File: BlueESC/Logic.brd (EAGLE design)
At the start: 24.4 x 27.5 mm, 33 parts, among them U1 ATMEGA168, U2 V_REG_LDOSMD, Y1 RESONATORSMD

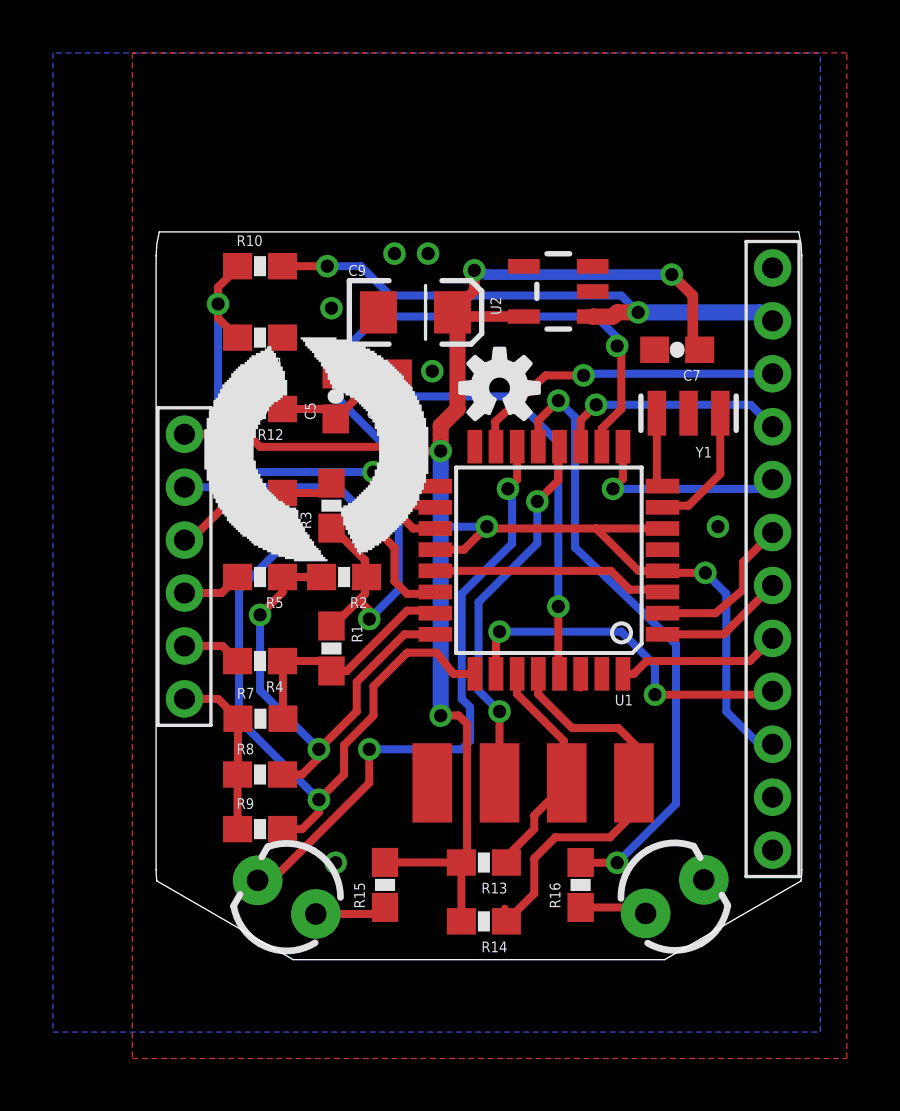
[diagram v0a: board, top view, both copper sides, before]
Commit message: Switch to SMT LEDs.
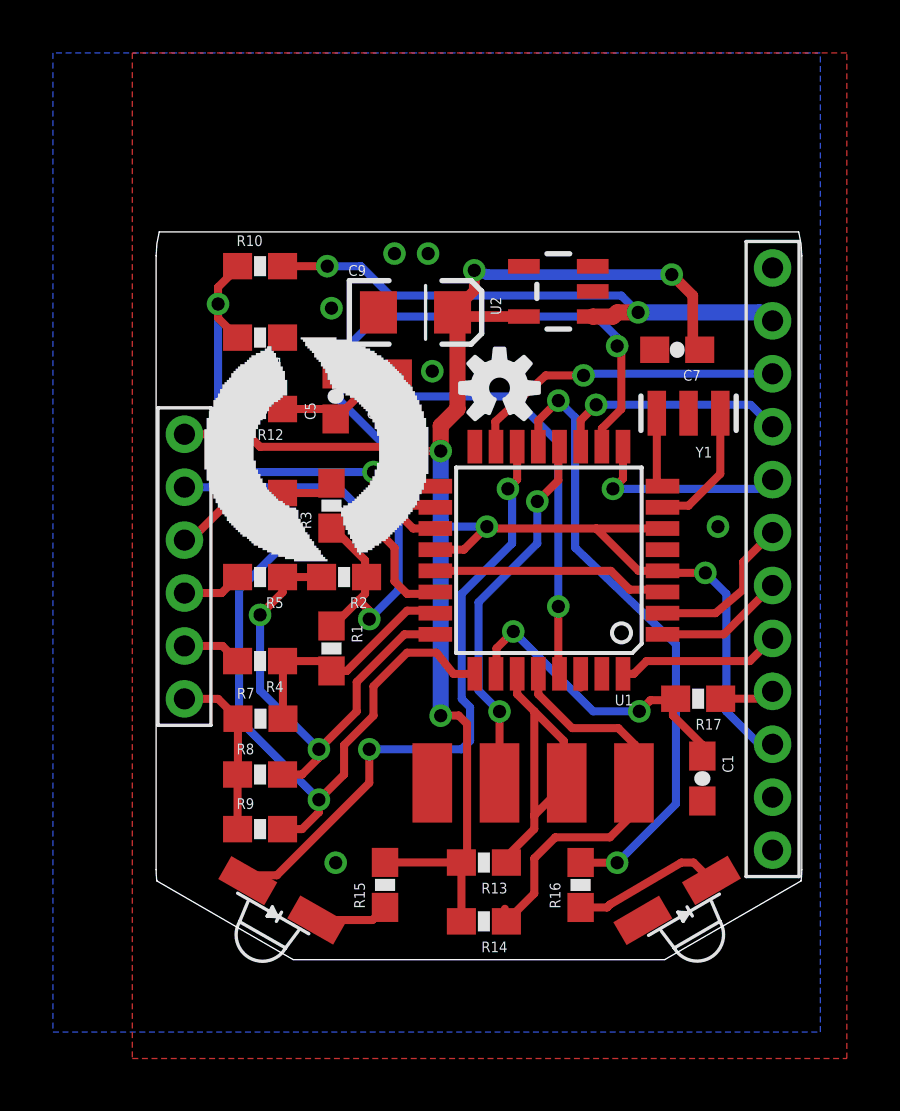
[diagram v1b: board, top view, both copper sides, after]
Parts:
- added C1: 1uF, SparkFun-Capacitors:0603-CAP
- added R17: 47K, SparkFun:0603-RES
- LED1: value RED -> BLUE; device SparkFun:LED3MM -> BR-Eagle-Library:SMT-LED-3X2-RA
- LED2: value BLUE -> RED; device SparkFun:LED3MM -> BR-Eagle-Library:SMT-LED-3X2-RA
- R15: value 2.2K -> 1K
- R16: value 150 -> 10K
- moved LED1 14.8 mm to (4.76, 5.24), turned to 150.3 degrees
- moved LED2 14.8 mm to (19.7, 5.24), turned to 210.2 degrees
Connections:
- new net CURRENT_ADC_FILTERED: C1.1, R17.2, U1.26
- net CURRENT_ADC: now also R17.1; no longer U1.26
- net GND: now also C1.2, LED2.2; no longer LED1.K
- net LED_STATUS: now also LED1.2; no longer LED2.K
- net N$16: now also LED1.1; no longer LED2.A
- net N$3: now also LED2.1; no longer LED1.A
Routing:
- net CURRENT_ADC_FILTERED: track 0.00 -> 12.0 mm, vias 0 -> 2
- net CURRENT_ADC: track 13.7 -> 2.08 mm, vias 2 -> 0
- net SDA: track 9.98 -> 13.9 mm
- net N$3: track 2.55 -> 5.70 mm
- net LED_STATUS: track 23.3 -> 24.2 mm
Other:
- board text added: "8/15"
- board text added: "BLUEESC-ELEC-LOGIC-R1.1"
- board text added: "Designed by R. Jehangir"
- board text added: "ERROR"
- board text added: "STATUS"
- board text added: "rev6"
- board text removed: "1/15"
- board text removed: "BLUESC-ELEC-LOGIC-X1B"
- board text removed: "Designed by R.J."
- board text removed: "rev5"

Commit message: Added PWM pull-down resistor.
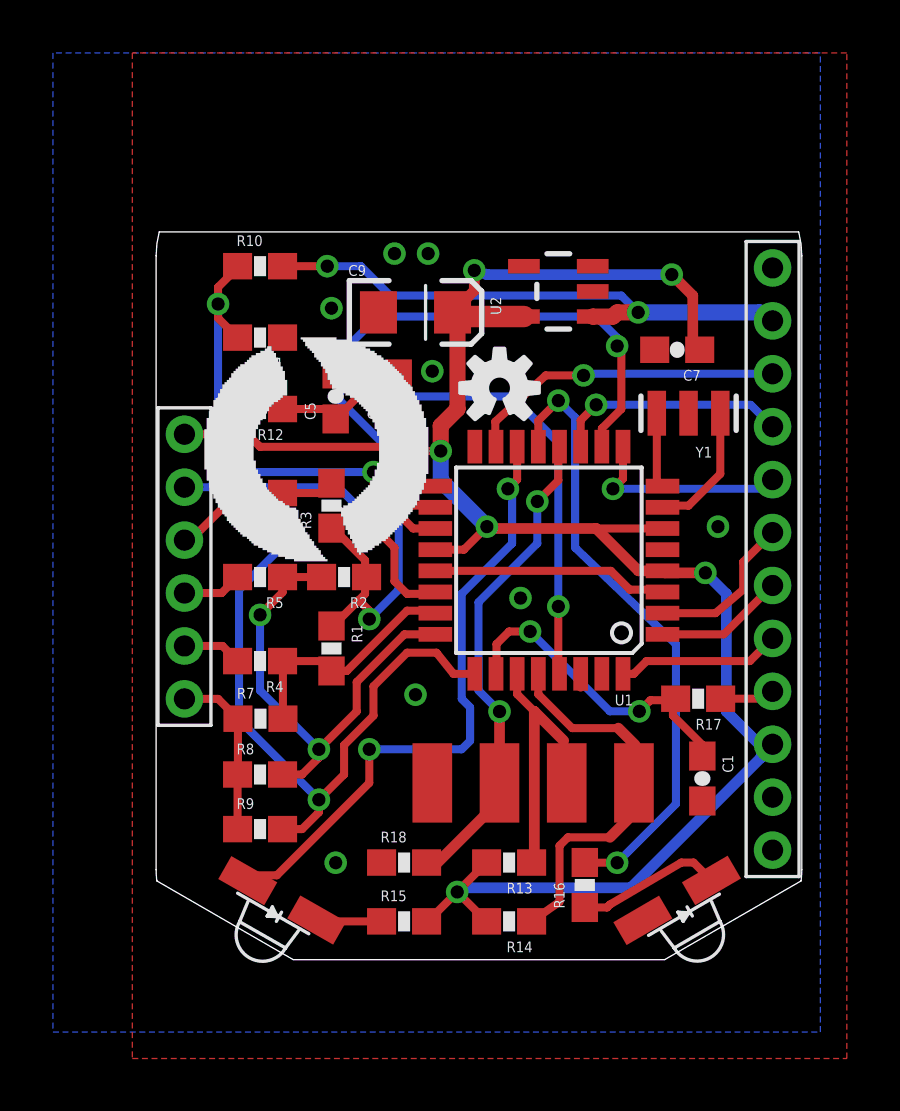
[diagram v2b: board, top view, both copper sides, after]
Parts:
- added R18: 10K, SparkFun:0603-RES
- moved R15 1.55 mm to (9.37, 4.45), turned to 0 degrees
- moved R13 0.95 mm to (13.3, 6.67)
- moved R14 0.95 mm to (13.3, 4.45)
- moved R16 0.16 mm to (16.2, 5.82)
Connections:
- net GND: now also R18.1
- net PWM: now also R18.2
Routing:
- net PWM: track 14.3 -> 18.7 mm
- net SDA: track 13.9 -> 11.8 mm
- net SCL: track 15.6 -> 14.6 mm
- net VCC5V: track 81.6 -> 80.9 mm
- net N$16: track 3.13 -> 2.47 mm
- net GND: vias 6 -> 8
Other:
- board text removed: "ERROR"
- board text removed: "STATUS"

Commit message: New logic board prototype ordered 8/14/15.
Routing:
- net VCC5V: track 80.9 -> 87.2 mm
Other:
- board text added: "BLK"
- board text added: "GRN"
- board text added: "R/Y"
- board text added: "WHT"
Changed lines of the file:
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@@
 <plain>
 <text x="9.04875" y="4.92125" size="0.6096" layer="52" rot="MR90">BLUEESC-ELEC-LOGIC-R1.1</text>
-<text x="11.38555" y="11.8999" size="0.6096" layer="51" rot="R180">GND</text>
-<text x="13.92555" y="11.8999" size="0.6096" layer="51" rot="R180">PWM</text>
-<text x="16.46555" y="11.8999" size="0.6096" layer="51" rot="R180">SDA</text>
-<text x="19.00555" y="11.8999" size="0.6096" layer="51" rot="R180">SCL</text>
+<text x="11.38555" y="11.8999" size="0.6096" layer="51" rot="R180">BLK</text>
+<text x="13.92555" y="11.8999" size="0.6096" layer="51" rot="R180">R/Y</text>
+<text x="16.46555" y="11.8999" size="0.6096" layer="51" rot="R180">WHT</text>
+<text x="19.00555" y="11.8999" size="0.6096" layer="51" rot="R180">GRN</text>
 <text x="15.83055" y="4.9149" size="0.8128" layer="52" rot="MR90">BlueRobotics</text>
 <text x="14.24305" y="4.9149" size="0.6096" layer="52" rot="MR90">Designed by R. Jehangir</text>
@@
 <wire x1="10.21625" y1="4.445" x2="10.2625" y2="4.445" width="0.3048" layer="1"/>
 <wire x1="10.2625" y1="4.445" x2="11.37375" y2="5.55625" width="0.3048" layer="1"/>
+<wire x1="13.6525" y1="26.51125" x2="11.7475" y2="26.51125" width="1.016" layer="1"/>
+<wire x1="13.81125" y1="27.14625" x2="13.81125" y2="25.7175" width="1.016" layer="1"/>
+<wire x1="13.81125" y1="25.7175" x2="11.58875" y2="25.7175" width="1.016" layer="1"/>
+<wire x1="13.81125" y1="27.14625" x2="13.6525" y2="27.14625" width="1.016" layer="1"/>
+<wire x1="13.6525" y1="27.14625" x2="13.6525" y2="26.51125" width="1.016" layer="1"/>
+<wire x1="13.89545" y1="27.30115" x2="13.81125" y2="27.14625" width="0" layer="19" extent="1-1"/>
 </signal>
 <signal name="RX">

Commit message: Updated PWM pull down to 470K to avoid avoid beating out the internal pull-ups used in ArduinoUSBLinker.
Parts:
- R16: value 10K -> 4.7K
- R18: value 10K -> 470K
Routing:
- net N$16: track 2.47 -> 7.49 mm
- net N$3: track 5.54 -> 2.49 mm
- net LED_STATUS: track 24.2 -> 21.7 mm
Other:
- board text added: "9/15"
- board text added: "rev7"
- board text removed: "8/15"
- board text removed: "rev6"
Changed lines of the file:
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@@
 <?xml version="1.0" encoding="utf-8"?>
 <!DOCTYPE eagle SYSTEM "eagle.dtd">
-<eagle version="7.1.0">
+<eagle version="7.4.0">
 <drawing>
 <settings>
@@
 <setting verticaltext="up"/>
 </settings>
-<grid distance="0.05" unitdist="inch" unit="inch" style="lines" multiple="1" display="yes" altdistance="0.00625" altunitdist="inch" altunit="inch"/>
+<grid distance="1" unitdist="mm" unit="mm" style="lines" multiple="1" display="yes" altdistance="0.00625" altunitdist="inch" altunit="inch"/>
 <layers>
 <layer number="1" name="Top" color="4" fill="1" visible="yes" active="yes"/>
@@
 <text x="15.83055" y="4.9149" size="0.8128" layer="52" rot="MR90">BlueRobotics</text>
 <text x="14.24305" y="4.9149" size="0.6096" layer="52" rot="MR90">Designed by R. Jehangir</text>
-<text x="12.33805" y="4.9149" size="0.8128" layer="52" rot="MR90">8/15</text>
+<text x="12.33805" y="4.9149" size="0.8128" layer="52" rot="MR90">9/15</text>
 <text x="1.4986" y="6.53415" size="0.8128" layer="51" rot="R90">BlueESC</text>
 <text x="5.03555" y="5.8674" size="0.6096" layer="51" ratio="13">B</text>
@@
 <text x="16.46555" y="8.0899" size="0.6096" layer="51" rot="R180">SDA</text>
 <text x="19.00555" y="8.0899" size="0.6096" layer="51" rot="R180">SCL</text>
-<text x="1.3843" y="24.44115" size="0.8128" layer="51" ratio="13" rot="R90">rev6</text>
+<text x="1.3843" y="24.44115" size="0.8128" layer="51" ratio="13" rot="R90">rev7</text>
 <wire x1="-0.003740625" y1="29.59865" x2="-0.003740625" y2="6.39865" width="0" layer="20"/>
 <wire x1="0.11395" y1="30.49865" x2="-0.00374375" y2="29.59865" width="0" layer="20" curve="14.900586"/>
@@
 <element name="R14" library="SparkFun-Resistors" package="0603-RES" value="10K" x="13.335" y="4.445" rot="R180"/>
 <element name="R15" library="SparkFun" package="0603-RES" value="1K" x="9.36625" y="4.445"/>
-<element name="R16" library="SparkFun" package="0603-RES" value="10K" x="16.19555" y="5.8199" rot="R90"/>
+<element name="R16" library="SparkFun" package="0603-RES" value="4.7K" x="16.19555" y="5.8199" rot="R90"/>
 <element name="R2" library="SparkFun-Resistors" package="0603-RES" value="47K" x="7.0993" y="17.45615" rot="R180"/>
 <element name="R3" library="SparkFun-Resistors" package="0603-RES" value="47K" x="6.62305" y="20.1549" rot="R90"/>
@@
 <element name="LED1" library="BR-Eagle-Library" package="SMT-LED-3X2-RA" value="BLUE" x="4.7625" y="5.23875" rot="R150.3"/>
 <element name="LED2" library="BR-Eagle-Library" package="SMT-LED-3X2-RA" value="RED" x="19.685" y="5.23875" rot="R210.2"/>
-<element name="R18" library="SparkFun" package="0603-RES" value="10K" x="9.36625" y="6.6675"/>
+<element name="R18" library="SparkFun" package="0603-RES" value="470K" x="9.36625" y="6.6675"/>
 </elements>
 <signals>
@@
 <via x="21.22805" y="19.36115" extent="1-16" drill="0.5"/>
 <via x="6.62305" y="27.61615" extent="1-16" drill="0.5"/>
-<via x="6.7818" y="6.66115" extent="1-16" drill="0.5"/>
+<via x="8.4643" y="10.56615" extent="1-16" drill="0.5"/>
 <via x="10.43305" y="25.2349" extent="1-16" drill="0.5"/>
 <via x="9.0043" y="29.6799" extent="1-16" drill="0.5"/>
@@
 <wire x1="10.2625" y1="4.445" x2="11.37375" y2="5.55625" width="0.3048" layer="1"/>
 <wire x1="13.6525" y1="26.51125" x2="11.7475" y2="26.51125" width="1.016" layer="1"/>
-<wire x1="13.81125" y1="27.14625" x2="13.81125" y2="25.7175" width="1.016" layer="1"/>
+<wire x1="13.81125" y1="27.14625" x2="13.81125" y2="27" width="1.016" layer="1"/>
+<wire x1="13.81125" y1="27" x2="13.81125" y2="25.7175" width="1.016" layer="1"/>
 <wire x1="13.81125" y1="25.7175" x2="11.58875" y2="25.7175" width="1.016" layer="1"/>
 <wire x1="13.81125" y1="27.14625" x2="13.6525" y2="27.14625" width="1.016" layer="1"/>
 <wire x1="13.6525" y1="27.14625" x2="13.6525" y2="26.51125" width="1.016" layer="1"/>
-<wire x1="13.89545" y1="27.30115" x2="13.81125" y2="27.14625" width="0" layer="19" extent="1-1"/>
+<wire x1="13.89545" y1="27.30115" x2="13.89545" y2="27.0842" width="0.3048" layer="1"/>
+<wire x1="13.89545" y1="27.0842" x2="13.81125" y2="27" width="0.3048" layer="1"/>
 </signal>
 <signal name="RX">
@@
 <wire x1="11.8618" y1="12.5349" x2="11.8618" y2="11.2649" width="0.3048" layer="16"/>
 <wire x1="11.8618" y1="11.2649" x2="11.5443" y2="10.9474" width="0.3048" layer="16"/>
-<wire x1="11.5443" y1="10.9474" x2="8.0518" y2="10.9474" width="0.3048" layer="16"/>
-<via x="8.0518" y="10.9474" extent="1-16" drill="0.5"/>
-<wire x1="8.0518" y1="10.9474" x2="8.0518" y2="9.6774" width="0.3048" layer="1"/>
-<wire x1="8.0518" y1="9.6774" x2="4.5593" y2="6.1849" width="0.3048" layer="1"/>
 <contactref element="LED1" pad="2"/>
-<wire x1="4.5593" y1="6.1849" x2="3.14205" y2="6.1849" width="0.3048" layer="1"/>
-<wire x1="3.14205" y1="6.1849" x2="3.45955" y2="5.9819375" width="0.3048" layer="1"/>
+<wire x1="11.5443" y1="10.9474" x2="11.10615" y2="10.9474" width="0.3048" layer="16"/>
+<wire x1="11.10615" y1="10.9474" x2="6.19125" y2="6.0325" width="0.3048" layer="16"/>
+<via x="6.19125" y="6.0325" extent="1-16" drill="0.5"/>
+<wire x1="6.19125" y1="6.0325" x2="6.19125" y2="4.6213625" width="0.3048" layer="1"/>
+<wire x1="6.19125" y1="4.6213625" x2="6.065446875" y2="4.495559375" width="0.3048" layer="1"/>
 </signal>
 <signal name="TEMP_ADC">
@@
 <contactref element="R15" pad="1"/>
 <contactref element="LED1" pad="1"/>
-<wire x1="8.51625" y1="4.445" x2="6.11600625" y2="4.445" width="0.3048" layer="1"/>
-<wire x1="6.11600625" y1="4.445" x2="6.065446875" y2="4.495559375" width="0.3048" layer="1"/>
+<wire x1="8.51625" y1="4.445" x2="8.255" y2="4.445" width="0.3048" layer="1"/>
+<wire x1="8.255" y1="4.445" x2="7.3025" y2="5.3975" width="0.3048" layer="1"/>
+<wire x1="7.3025" y1="5.3975" x2="7.3025" y2="6.82625" width="0.3048" layer="1"/>
+<wire x1="7.3025" y1="6.82625" x2="6.985" y2="7.14375" width="0.3048" layer="1"/>
+<wire x1="6.985" y1="7.14375" x2="5.715" y2="7.14375" width="0.3048" layer="1"/>
+<wire x1="5.715" y1="7.14375" x2="4.7625" y2="6.19125" width="0.3048" layer="1"/>
+<wire x1="4.7625" y1="6.19125" x2="3.6688625" y2="6.19125" width="0.3048" layer="1"/>
+<wire x1="3.6688625" y1="6.19125" x2="3.45955" y2="5.9819375" width="0.3048" layer="1"/>
 </signal>
 <signal name="N$3">
@@
 <wire x1="16.19555" y1="4.9699" x2="17.0349" y2="4.9699" width="0.3048" layer="1"/>
 <wire x1="17.0349" y1="4.9699" x2="17.145" y2="5.08" width="0.3048" layer="1"/>
-<wire x1="17.145" y1="5.08" x2="19.84375" y2="6.6675" width="0.3048" layer="1"/>
-<wire x1="19.84375" y1="6.6675" x2="20.3071875" y2="6.6675" width="0.3048" layer="1"/>
-<wire x1="20.3071875" y1="6.6675" x2="20.981409375" y2="5.993278125" width="0.3048" layer="1"/>
+<wire x1="17.145" y1="5.08" x2="17.79280625" y2="5.08" width="0.3048" layer="1"/>
+<wire x1="17.79280625" y1="5.08" x2="18.3885875" y2="4.48421875" width="0.3048" layer="1"/>
 </signal>
 <signal name="RESET">
